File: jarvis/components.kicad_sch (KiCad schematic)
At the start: 4 parts, among them IC2 MAX98357AETE+T, IC5 W25Q128JWSIQ, J1 Conn_01x02 - Speaker, J2 Mic Conn_01x05

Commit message: crystals done
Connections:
- net +3.3 is gone; now on net +3.3V: J2.4 (Pin_4)
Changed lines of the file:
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@@
 (kicad_sch
-	(version 20231120)
+	(version 20250114)
 	(generator "eeschema")
-	(generator_version "8.0")
+	(generator_version "9.0")
 	(paper "A4")
 	(wire
@@
 	(label "GND"
 		(at 140.97 81.28 180)
-		(effects
-			(font
-				(size 1.27 1.27)
-			)
-			(justify right bottom)
-		)
-	)
-	(label "+3.3"
-		(at 81.28 99.06 90)
-		(effects
-			(font
-				(size 1.27 1.27)
-			)
-			(justify left bottom)
-		)
-	)
-	(label "+3.3V"
-		(at 140.97 83.82 180)
 		(effects
 			(font
@@
 	)
 	(symbol
+		(lib_id "power:+3.3V")
+		(at 81.28 99.06 0)
+		(unit 1)
+		(exclude_from_sim no)
+		(in_bom yes)
+		(on_board yes)
+		(dnp no)
+		(property "Reference" "#PWR035"
+			(at 81.28 102.87 0)
+			(effects
+				(font
+					(size 1.27 1.27)
+				)
+				(hide yes)
+			)
+		)
+		(property "Value" "+3.3V"
+			(at 81.026 92.71 90)
+			(effects
+				(font
+					(size 1.27 1.27)
+				)
+			)
+		)
+		(property "Footprint" ""
+			(at 81.28 99.06 0)
+			(effects
+				(font
+					(size 1.27 1.27)
+				)
+				(hide yes)
+			)
+		)
+		(property "Datasheet" ""
+			(at 81.28 99.06 0)
+			(effects
+				(font
+					(size 1.27 1.27)
+				)
+				(hide yes)
+			)
+		)
+		(property "Description" "Power symbol creates a global label with name \"+3.3V\""
+			(at 81.28 99.06 0)
+			(effects
+				(font
+					(size 1.27 1.27)
+				)
+				(hide yes)
+			)
+		)
+		(pin "1"
+		)
+		(instances
+			(project "jarvis"
+				(path "/d21d45e5-a4fd-47b9-acaa-6ca2c284b61a/67d093e5-852b-486a-8803-27c9e57204b4"
+					(reference "#PWR035")
+					(unit 1)
+				)
+			)
+		)
+	)
+	(symbol
 		(lib_id "jarvis:W25Q128JWSIQ-1.8")
 		(at 128.27 133.35 0)
@@
 					(unit 1)
 				)
+			)
+		)
+	)
+	(symbol
+		(lib_id "power:+3.3V")
+		(at 140.97 83.82 90)
+		(unit 1)
+		(exclude_from_sim no)
+		(in_bom yes)
+		(on_board yes)
+		(dnp no)
+		(property "Reference" "#PWR036"
+			(at 144.78 83.82 0)
+			(effects
+				(font
+					(size 1.27 1.27)
+				)
+				(hide yes)
+			)
+		)
+		(property "Value" "+3.3V"
+			(at 134.62 84.074 90)
+			(effects
+				(font
+					(size 1.27 1.27)
+				)
+			)
+		)
+		(property "Footprint" ""
+			(at 140.97 83.82 0)
+			(effects
+				(font
+					(size 1.27 1.27)
+				)
+				(hide yes)
+			)
+		)
+		(property "Datasheet" ""
+			(at 140.97 83.82 0)
+			(effects
+				(font
+					(size 1.27 1.27)
+				)
+				(hide yes)
+			)
+		)
+		(property "Description" "Power symbol creates a global label with name \"+3.3V\""
+			(at 140.97 83.82 0)
+			(effects
+				(font
+					(size 1.27 1.27)
+				)
+				(hide yes)
+			)
+		)
+		(pin "1"
+		)
+		(instances
+			(project "jarvis"
+				(path "/d21d45e5-a4fd-47b9-acaa-6ca2c284b61a/67d093e5-852b-486a-8803-27c9e57204b4"
+					(reference "#PWR036")
+					(unit 1)
+				)

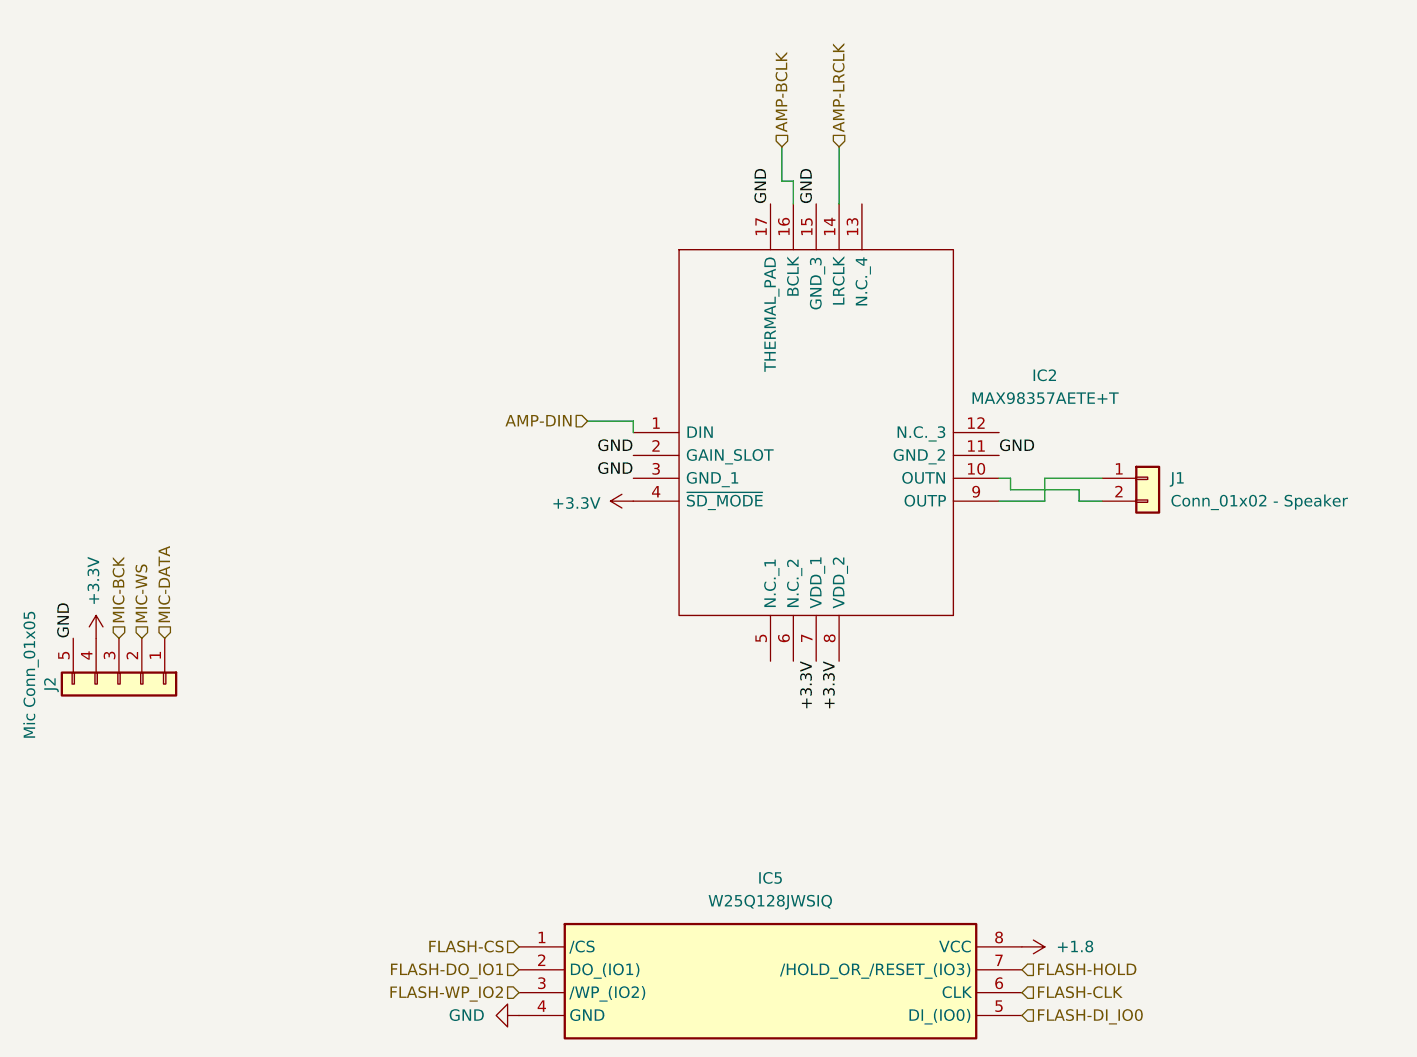
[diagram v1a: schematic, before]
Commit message: with leds and boot button
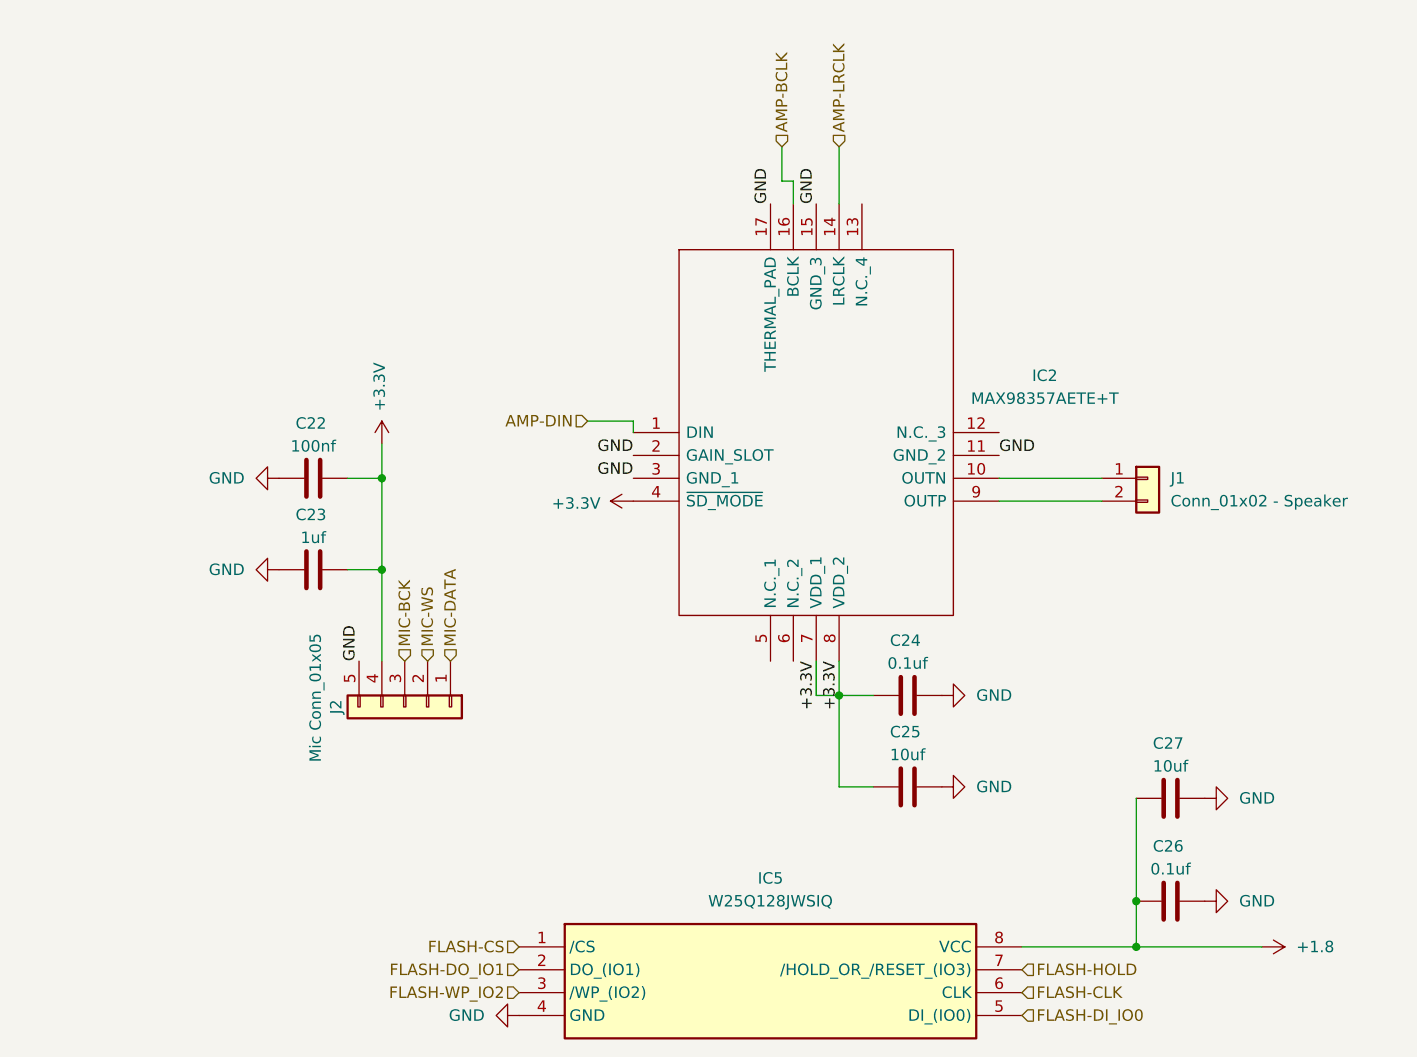
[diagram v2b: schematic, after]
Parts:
- added C22: 100nf, Capacitor_SMD:C_0603_1608Metric, symbol Device:C
- added C23: 1uf, Capacitor_SMD:C_0603_1608Metric, symbol Device:C
- added C24, C26: 0.1uf, Capacitor_SMD:C_0603_1608Metric, symbol Device:C
- added C25, C27: 10uf, Capacitor_SMD:C_0603_1608Metric, symbol Device:C
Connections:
- net +1.8: now also C26.2, C27.2
- net +3.3V: now also C22.1, C23.1, C24.2, C25.2
- net GND: now also C22.2, C23.2, C24.1, C25.1, C26.1, C27.1
- net at IC2.10 (OUTN): now also J1.1 (Pin_1); no longer J1.2 (Pin_2)
- net at IC2.9 (OUTP): now also J1.2 (Pin_2); no longer J1.1 (Pin_1)
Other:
- moved on the sheet: J2
